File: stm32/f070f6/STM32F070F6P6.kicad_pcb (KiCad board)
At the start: 2 copper layers, 29 parts, among them J1 STLINK, J2 USB_C_REC_16PIN, J3 L, J4 L, SW1 BOOT0, U1 XC6220B331MR, U2 STM32F070F6Px, Y1 8 MHz

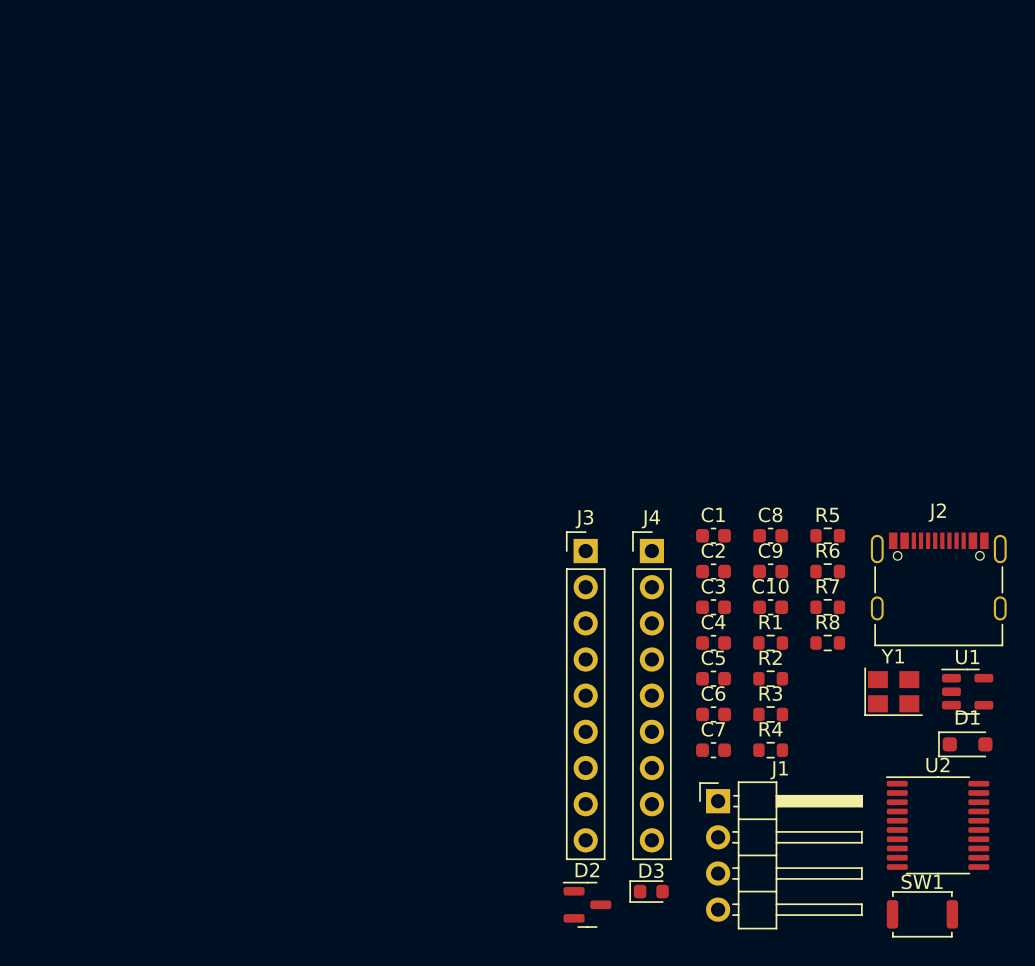
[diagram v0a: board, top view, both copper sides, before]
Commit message: Update: Artwork completed for `F070F6P6`.
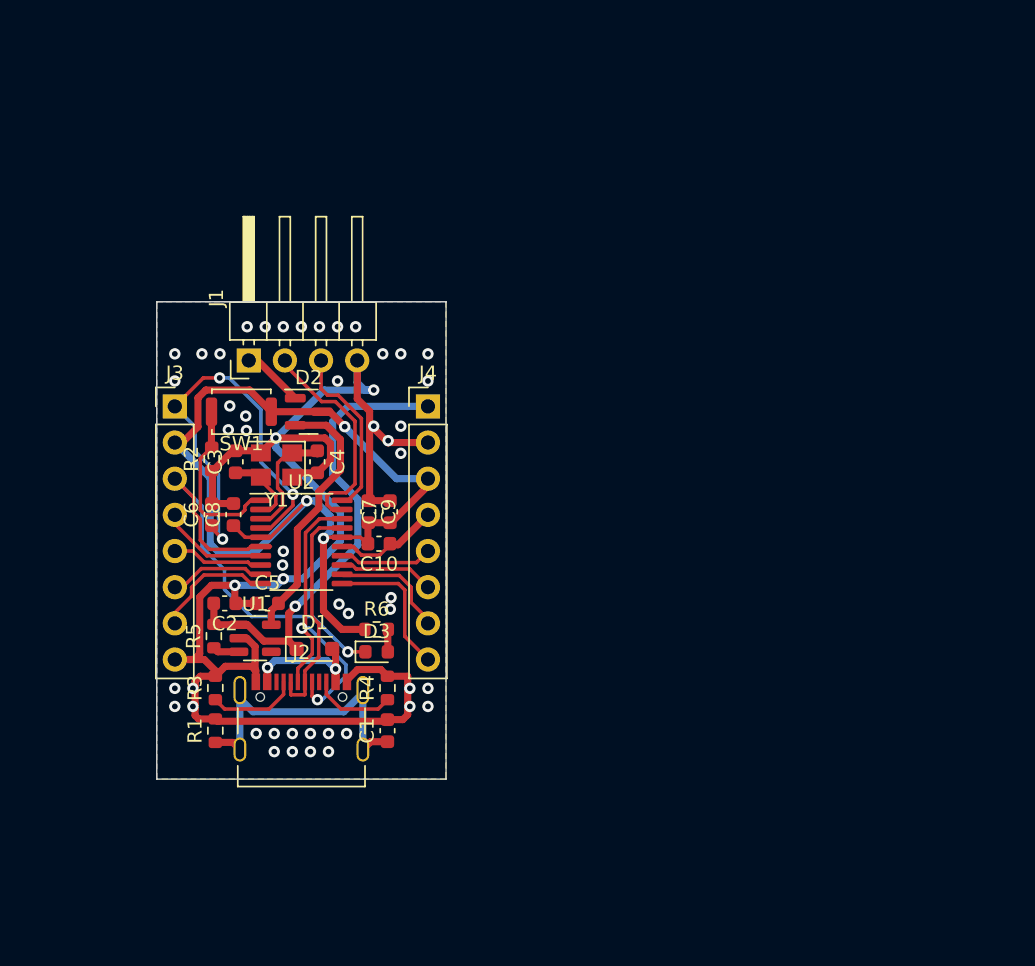
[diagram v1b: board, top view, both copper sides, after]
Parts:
- removed R7: 0, Resistor_SMD:R_0603_1608Metric
- removed R8: 1k, Resistor_SMD:R_0603_1608Metric
- J3, J4: footprint Connector_PinHeader_2.54mm:PinHeader_1x09_P2.54mm_Vertical -> Connector_PinHeader_2.54mm:PinHeader_1x08_P2.54mm_Vertical
- R6: value 0 -> 1k
- moved SW1 59.5 mm to (40.2, 47.2), turned to 180 degrees
- moved U1 50.2 mm to (41.2, 63.2)
- moved U2 49.0 mm to (44.5, 56.4)
- moved D1 46.4 mm to (45.4, 63.9)
- moved Y1 46.2 mm to (42.7, 51.0), turned to 180 degrees
- moved J2 45.9 mm to (44.5, 68.7)
- moved J1 45.2 mm to (40.8, 43.6), turned to 90 degrees
- moved R5 43.7 mm to (38.3, 63.0), turned to 90 degrees
- moved R2 42.2 mm to (38.2, 50.6), turned to 90 degrees
- moved D2 39.8 mm to (45.0, 47.2)
- moved R1 39.5 mm to (38.4, 69.6), turned to 90 degrees
- moved R3 39.0 mm to (38.4, 66.6), turned to 90 degrees
- moved C6 37.9 mm to (38.2, 54.5), turned to 90 degrees
- moved C8 37.8 mm to (39.7, 54.5), turned to 90 degrees
- moved C3 35.1 mm to (39.8, 50.8), turned to 90 degrees
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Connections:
- C6 pad 1: Net-(U2-NRST) -> NRST
- J3 pad 1: +5V -> NRST
- J3 pad 2: NRST -> +3.3V
- J3 pad 3: +3.3V -> PA0
- J3 pad 4: PA0 -> PA1
- J3 pad 5: PA1 -> PA2
- J3 pad 6: PA2 -> PA3
- J3 pad 7: PA3 -> PA4
- J3 pad 8: PA4 -> GND
- J4 pad 4: +3.3V -> GND
- J4 pad 5: GND -> PB1
- J4 pad 6: PB1 -> PA7
- J4 pad 7: PA7 -> PA6
- J4 pad 8: PA6 -> PA5
- R6 pad 1: PA13 -> +3.3V
- R6 pad 2: SWDIO -> Net-(D3-A)
- U2 pad 4: Net-(U2-NRST) -> NRST
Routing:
- net GND: track 0.00 -> 121.4 mm, vias 0 -> 52
- net +3.3V: track 0.00 -> 69.5 mm, vias 0 -> 3
- net +5V: track 0.00 -> 33.4 mm, vias 0 -> 1
- net PA0: track 0.00 -> 31.3 mm, vias 0 -> 1
- net NRST: track 0.00 -> 30.4 mm, vias 0 -> 3
- net USB_DP: track 0.00 -> 23.2 mm, vias 0 -> 2
- net Net-(J2-SHIELD): track 0.00 -> 22.6 mm
- net +3.3VA: track 0.00 -> 18.6 mm
- net USB_DM: track 0.00 -> 16.0 mm
- net SWDIO: track 0.00 -> 15.4 mm
- net SWCLK: track 0.00 -> 12.5 mm
- net BOOT0: track 0.00 -> 12.2 mm
- net PA5: track 0.00 -> 10.1 mm
- net Net-(D1-A): track 0.00 -> 9.57 mm, vias 0 -> 2
- net PA4: track 0.00 -> 8.48 mm
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- added copper zone on B.Cu, net GND
- added copper zone on F.Cu, net GND
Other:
- board outline added: 20.3 x 33.5 mm

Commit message: Update 2023-11-27
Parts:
- removed SW1: BOOT0, Button_Switch_SMD:SW_Push_SPST_NO_Alps_SKRK
- J3, J4: footprint Connector_PinHeader_2.54mm:PinHeader_1x08_P2.54mm_Vertical -> Connector_PinSocket_2.54mm:PinSocket_1x10_P2.54mm_Vertical
- moved R4 45.0 mm to (30.5, 26.4), turned to -90 degrees
- moved C1 44.9 mm to (30.5, 29.5), turned to -90 degrees
- moved J2 42.9 mm to (36.8, 26.5), turned to 180 degrees
- moved R3 40.6 mm to (43.2, 26.4), turned to -90 degrees
- moved R1 40.5 mm to (43.2, 29.5), turned to -90 degrees
- moved D1 33.1 mm to (38.6, 31.5)
- moved U1 31.5 mm to (33.3, 32.6), turned to -90 degrees
- moved C2 28.8 mm to (35.8, 32.1), turned to 90 degrees
- moved R5 27.8 mm to (33.3, 35.7), turned to 0 degrees
- moved C5 26.3 mm to (35.8, 35.2), turned to -90 degrees
- moved D3 26.2 mm to (29.9, 47.0), turned to -90 degrees
- moved J3 24.4 mm to (26.7, 24.1)
- moved J4 23.6 mm to (47.0, 24.1)
- moved C6 19.3 mm to (37.3, 35.2)
- moved C3 18.6 mm to (30.1, 34.9)
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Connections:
- J3 pad 1: NRST -> +3.3V
- J3 pad 2: +3.3V -> BOOT0
- J3 pad 3: PA0 -> NRST
- J3 pad 4: PA1 -> +3.3V
- J3 pad 5: PA2 -> PA0
- J3 pad 6: PA3 -> PA1
- J3 pad 7: PA4 -> PA2
- J3 pad 8: GND -> PA3
- J4 pad 2: GND -> +5V
- J4 pad 3: +3.3V -> GND
- J4 pad 4: GND -> +3.3V
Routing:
- net Net-(D3-A): track 1.59 -> 14.8 mm
- net +3.3V: track 69.5 -> 79.6 mm, vias 3 -> 2
- net NRST: track 30.4 -> 20.3 mm, vias 3 -> 2
- net BOOT0: track 12.2 -> 22.3 mm, vias 0 -> 3
- net +3.3VA: track 18.6 -> 26.6 mm, vias 0 -> 2
- net GND: track 121.4 -> 128.8 mm, vias 52 -> 50
- net +5V: track 33.4 -> 26.6 mm, vias 1 -> 2
- net PA0: track 31.3 -> 25.0 mm, vias 1 -> 0
- net PB1: track 6.56 -> 12.6 mm
- net USB_DM: track 16.0 -> 20.7 mm
- net PA1: track 7.59 -> 12.1 mm
- net USB_DP: track 23.2 -> 18.8 mm
- net PA7: track 6.67 -> 10.7 mm
- net SWDIO: track 15.4 -> 11.4 mm, vias 0 -> 2
- net HSE_OUT: track 8.22 -> 4.27 mm
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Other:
- board size 20.3 x 33.5 mm -> 22.9 x 28.9 mm
